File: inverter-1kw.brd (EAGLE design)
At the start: 160 x 100 mm, 240 parts, among them IC1 LM358D, IC5 ISO3082, IC6 25LC080SN, IC9 LM358D, Q2 1200980569**TRANS SMD NPN MMB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, Q3 1200980569**TRANS SMD NPN MMB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, Q4 1200980569**TRANS SMD NPN MMB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, Q6 1200980569**TRANS SMD NPN MMB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, U1 ACS712, U2 STM32F334C6, U3 1039-2088**AM1L-0505SH30-NZ A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, U4 ACS712, U5 SI8230, U6 SI8230, U7 ACS712, X1 MCV3, X2 RADE2, X3 RADE2, X7 RADE2, X8 RADE2

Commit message: Giriş kondansatörleri düzenlendi.
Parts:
- moved R41 300.2 mm to (103.1, 71.3)
- moved R36 287.5 mm to (97.6, 69.2), turned to 90 degrees
- moved C31 285.4 mm to (144.4, 90.2), turned to 90 degrees
- moved Q4 264.9 mm to (88.3, 70.0)
- moved C32 219.8 mm to (52.4, 90.1), turned to 90 degrees
- moved C73 209.5 mm to (39.3, 66.9), turned to 270 degrees
- moved C72 207.7 mm to (41.9, 66.9), turned to 270 degrees
- moved R60 197.4 mm to (39.8, 69.9)
- moved R59 192.9 mm to (39.8, 71.6)
- moved C40 185.0 mm to (88.9, 90.2), turned to 90 degrees
- moved Q6 183.6 mm to (109.3, 71.0)
- moved C35 181.0 mm to (107.8, 90.2), turned to 90 degrees
- moved C34 176.4 mm to (126.0, 90.2), turned to 90 degrees
- moved X8 165.2 mm to (2.34, 77.1), turned to 180 degrees
- moved X7 155.9 mm to (2.21, 87.9), turned to 180 degrees
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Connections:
- removed net 400V-: U4.3, U4.4, X8.1, X8.2
- new net N$31: R94.1, R95.2
- new net N$32: R95.1, R96.2
- new net N$4: R93.1, R94.2
- new net V+: C83.1, C84.1, GN1.D, R65.2, R72.2, R74.2, R93.2, U4.3, U4.4
- net AGND: now also R96.1, X8.1, X8.2; no longer U4.1, U4.2
- net V_IN: now also U4.1, U4.2; no longer C83.1, C84.1, GN1.D, R65.2, R72.2, R74.2
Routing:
- net VDIG+: track 0.00 -> 34.5 mm
- net N$55: track 0.00 -> 34.0 mm
- net +12V: track 0.00 -> 30.3 mm, vias 0 -> 1
- net N$51: track 0.00 -> 25.5 mm
- net V_IN: track 0.00 -> 16.6 mm
- net N$44: track 0.00 -> 8.48 mm
- net N$69: track 0.00 -> 6.78 mm
- net N$70: track 0.00 -> 5.66 mm
- net DGND: track 0.00 -> 5.32 mm
- added copper zone on layer 1, net V_IN

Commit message: Bobin paketleri guncellendi. Roleler ince secildi.
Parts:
- added R97, R98: (no value), rcl:R1206
- L1, L2: value SFT830D -> SFT1240; device inductors:SFT830D -> inductors:SFT1240
- RL1, RL2: value G5LE-TEK -> 0417; device Erelay:G5LE-TEK -> Erelay:0417
- moved RL1 201.7 mm to (-162.4, -5.21), turned to 0 degrees
- moved RL2 198.9 mm to (-162.4, -16.1), turned to 0 degrees
- moved L2 97.3 mm to (-202.3, -18.1)
- moved L1 91.6 mm to (-184.5, -18.1)
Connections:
- net N$32 renamed VIN_SENS
- removed net I_LEFT_AC: R47.1, U1.7, U7.7
- new net IA_SENS: U7.7
- new net IB_SENS: R47.1, U1.7
- new net VA_SENS: R25.1, R98.1
- new net VB_SENS: R87.1, R97.2
- net AGND: now also R97.1, R98.2
- net N$28: now also R87.2; no longer R87.1
- net N$55: now also RL1.O; no longer RL1.S
- net VDIG+: now also RL1.S; no longer RL1.P
- net V_IN: now also RL2.O; no longer RL2.P
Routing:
- net VDIG+: track 34.5 -> 0.00 mm
- net N$51: track 25.5 -> 20.4 mm
- net N$55: track 34.0 -> 29.4 mm
- net +12V: track 30.3 -> 26.8 mm
- net N$44: track 8.48 -> 7.83 mm

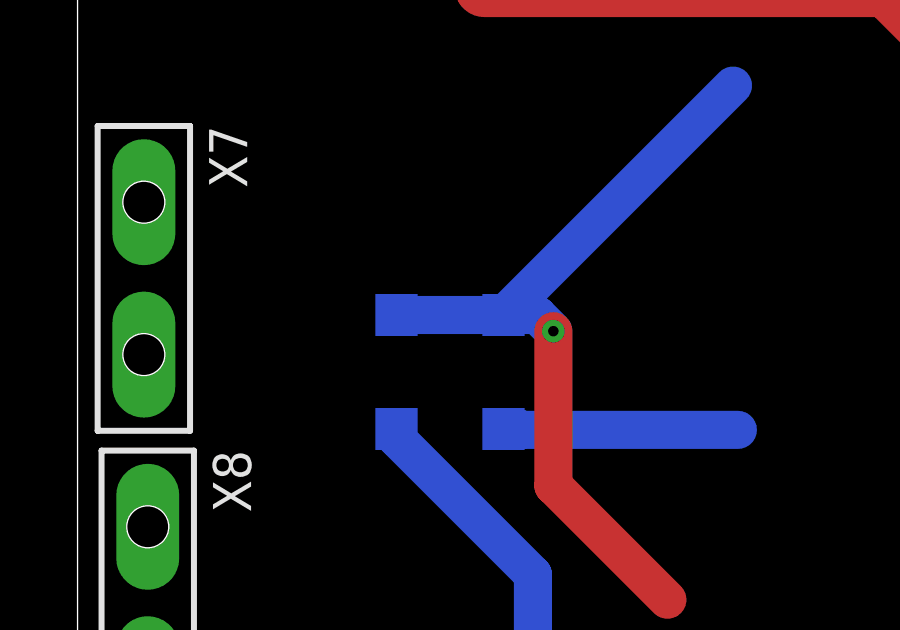
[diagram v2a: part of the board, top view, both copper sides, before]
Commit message: Role beslemeleri VDD ile sembolize edildi.
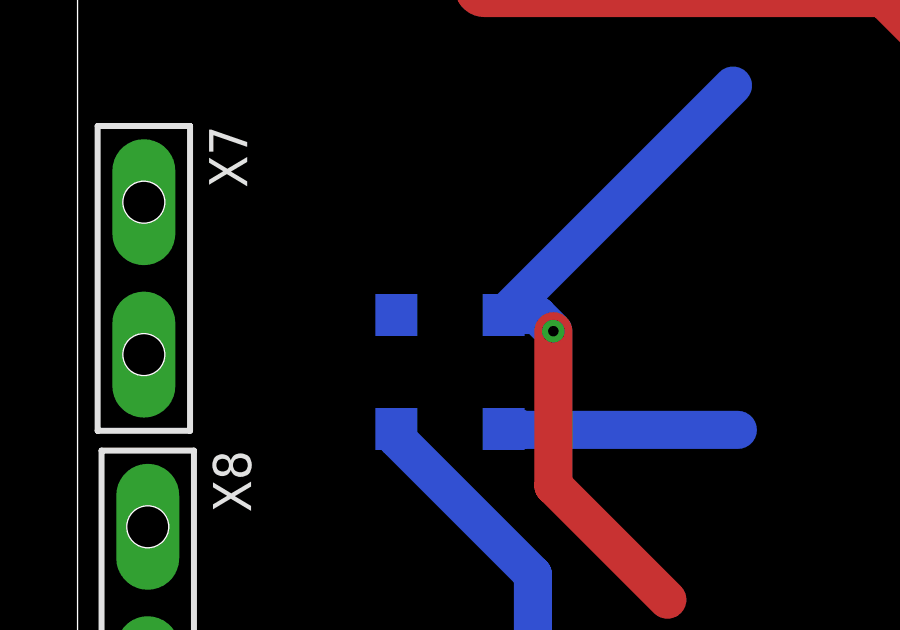
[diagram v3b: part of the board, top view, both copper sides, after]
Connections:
- net +12V renamed VDD
- net VDIG+ renamed VSUPPLY+
- removed net V+: C83.1, C84.1, GN1.D, R65.2, R72.2, R74.2, R93.2, U4.3, U4.4
- new net IIN_SENS: U4.7
- new net VIN: C83.1, C84.1, C95.1, C96.1, GN1.D, GN3.D, R65.2, R72.2, R74.2, R89.2, R91.2, R92.2, R93.2, U4.3, U4.4
- net I_LEFT_DC: no longer U4.7
- net V_IN: no longer C95.1, C96.1, GN3.D, R89.2, R91.2, R92.2
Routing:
- net VDD: track 26.8 -> 23.2 mm
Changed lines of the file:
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@@
 <contactref element="C35" pad="+"/>
 <contactref element="C40" pad="+"/>
-<contactref element="R89" pad="2"/>
-<contactref element="R91" pad="2"/>
-<contactref element="R92" pad="2"/>
-<contactref element="C95" pad="1"/>
-<contactref element="C96" pad="1"/>
-<contactref element="GN3" pad="D"/>
 <contactref element="U4" pad="1"/>
 <contactref element="U4" pad="2"/>
@@
 <wire x1="31.54" y1="69.155" x2="41.69" y2="82.49" width="0" layer="19" extent="1-1"/>
 <wire x1="31.54" y1="67.885" x2="31.54" y2="69.155" width="0" layer="19" extent="1-1"/>
-<wire x1="-123.013" y1="195.58" x2="41.72" y2="95.55" width="0" layer="19" extent="1-1"/>
-<wire x1="-135.713" y1="195.58" x2="-123.013" y2="195.58" width="0" layer="19" extent="1-1"/>
-<wire x1="-142.063" y1="195.58" x2="-135.713" y2="195.58" width="0" layer="19" extent="1-1"/>
-<wire x1="-113.16" y1="218.44" x2="-123.013" y2="195.58" width="0" layer="19" extent="1-1"/>
-<wire x1="-108.08" y1="218.44" x2="-113.16" y2="218.44" width="0" layer="19" extent="1-1"/>
-<wire x1="-163.995" y1="66.6" x2="-142.063" y2="195.58" width="0" layer="19" extent="1-1"/>
-<wire x1="-160.8525" y1="-19.7984" x2="-163.995" y2="66.6" width="0" layer="19" extent="1-1"/>
+<wire x1="-160.8525" y1="-19.7984" x2="31.54" y2="67.885" width="0" layer="19" extent="1-1"/>
 </signal>
 <signal name="GND_L">
@@
 <wire x1="-58.86" y1="87.65" x2="97.62" y2="70.23" width="0" layer="19" extent="1-1"/>
 </signal>
-<signal name="VDIG+">
+<signal name="VSUPPLY+">
 <contactref element="X7" pad="1"/>
 <contactref element="X7" pad="2"/>
@@
 </signal>
 <signal name="I_LEFT_DC">
-<contactref element="U4" pad="7"/>
 <contactref element="R61" pad="1"/>
-<wire x1="36.74" y1="67.885" x2="-88.48" y2="224.79" width="0" layer="19" extent="1-1"/>
-</signal>
-<signal name="+12V">
-<contactref element="D1" pad="C"/>
-<contactref element="D2" pad="C"/>
-<wire x1="14.2" y1="86.66" x2="21.849" y2="94.309" width="1.27" layer="16"/>
-<wire x1="19.663" y1="77.169" x2="15.86" y2="80.972" width="1.27" layer="1"/>
-<via x="15.86" y="86.12" extent="1-16" drill="0.35"/>
-<wire x1="15.86" y1="86.12" x2="15.32" y2="86.66" width="1.27" layer="16"/>
-<wire x1="15.32" y1="86.66" x2="14.2" y2="86.66" width="1.27" layer="16"/>
-<wire x1="15.86" y1="86.12" x2="15.86" y2="80.972" width="1.27" layer="1"/>
-<wire x1="10.63" y1="86.66" x2="14.2" y2="86.66" width="1.27" layer="16"/>
-<contactref element="RL1" pad="1"/>
-<contactref element="RL2" pad="1"/>
-<wire x1="-170.8982" y1="-8.9311" x2="-170.8982" y2="-19.8111" width="0" layer="19" extent="1-1"/>
-<wire x1="10.63" y1="86.66" x2="-170.8982" y2="-8.9311" width="0" layer="19" extent="16-16"/>
 </signal>
 <signal name="+15V">
@@
 <wire x1="-144.78" y1="85.09" x2="-144.78" y2="90.17" width="0" layer="19" extent="1-1"/>
 </signal>
-<signal name="V+">
+<signal name="VIN">
 <contactref element="R65" pad="2"/>
 <contactref element="R72" pad="2"/>
@@
 <contactref element="U4" pad="4"/>
 <contactref element="R93" pad="2"/>
+<contactref element="R89" pad="2"/>
+<contactref element="R91" pad="2"/>
+<contactref element="R92" pad="2"/>
+<contactref element="C95" pad="1"/>
+<contactref element="C96" pad="1"/>
+<contactref element="GN3" pad="D"/>
 <wire x1="-92.84" y1="218.44" x2="-87.76" y2="218.44" width="0" layer="19" extent="1-1"/>
+<wire x1="-108.08" y1="218.44" x2="-92.84" y2="218.44" width="0" layer="19" extent="1-1"/>
+<wire x1="-113.16" y1="218.44" x2="-108.08" y2="218.44" width="0" layer="19" extent="1-1"/>
 <wire x1="-84.913" y1="195.58" x2="-87.76" y2="218.44" width="0" layer="19" extent="1-1"/>
 <wire x1="-97.613" y1="195.58" x2="-84.913" y2="195.58" width="0" layer="19" extent="1-1"/>
 <wire x1="-103.963" y1="195.58" x2="-97.613" y2="195.58" width="0" layer="19" extent="1-1"/>
-<wire x1="-145.898" y1="218.44" x2="-103.963" y2="195.58" width="0" layer="19" extent="1-1"/>
-<wire x1="-119.94" y1="50.635" x2="-103.963" y2="195.58" width="0" layer="19" extent="1-1"/>
+<wire x1="-123.013" y1="195.58" x2="-103.963" y2="195.58" width="0" layer="19" extent="1-1"/>
+<wire x1="-135.713" y1="195.58" x2="-123.013" y2="195.58" width="0" layer="19" extent="1-1"/>
+<wire x1="-142.063" y1="195.58" x2="-135.713" y2="195.58" width="0" layer="19" extent="1-1"/>
+<wire x1="-145.898" y1="218.44" x2="-142.063" y2="195.58" width="0" layer="19" extent="1-1"/>
+<wire x1="-163.995" y1="66.6" x2="-142.063" y2="195.58" width="0" layer="19" extent="1-1"/>
+<wire x1="-119.94" y1="50.635" x2="-163.995" y2="66.6" width="0" layer="19" extent="1-1"/>
 <wire x1="31.54" y1="65.345" x2="-119.94" y2="50.635" width="0" layer="19" extent="1-1"/>
 <wire x1="31.54" y1="66.615" x2="31.54" y2="65.345" width="0" layer="19" extent="1-1"/>
@@
 <contactref element="U7" pad="7"/>
 </signal>
+<signal name="VDD">
+<contactref element="D1" pad="C"/>
+<contactref element="RL1" pad="1"/>
+<wire x1="14.2" y1="86.66" x2="21.849" y2="94.309" width="1.27" layer="16"/>
+<wire x1="19.663" y1="77.169" x2="15.86" y2="80.972" width="1.27" layer="1"/>
+<via x="15.86" y="86.12" extent="1-16" drill="0.35"/>
+<wire x1="15.86" y1="86.12" x2="15.32" y2="86.66" width="1.27" layer="16"/>
+<wire x1="15.32" y1="86.66" x2="14.2" y2="86.66" width="1.27" layer="16"/>
+<wire x1="15.86" y1="86.12" x2="15.86" y2="80.972" width="1.27" layer="1"/>
+<contactref element="D2" pad="C"/>
+<contactref element="RL2" pad="1"/>
+<wire x1="-170.8982" y1="-8.9311" x2="-170.8982" y2="-19.8111" width="0" layer="19" extent="1-1"/>
+<wire x1="10.63" y1="86.66" x2="-170.8982" y2="-8.9311" width="0" layer="19" extent="16-16"/>
+<wire x1="14.2" y1="86.66" x2="10.63" y2="86.66" width="0" layer="19" extent="16-16"/>
+</signal>
+<signal name="IIN_SENS">
+<contactref element="U4" pad="7"/>
+</signal>
 </signals>
